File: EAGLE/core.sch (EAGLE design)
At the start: 47 parts, among them Q1 MMDT3904, U1 MIC5219, U3 STM32F10XCXT6, U4 SST25VF040B-50-4I-S2AF, X1 USB-MICROB, Y1 8Mhz

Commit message: Integrated Satish's feedback
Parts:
- removed R10: 1K, SparkFun-Passives:RESISTOR0402-RES
- R3: value 1K -> 1K5
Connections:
- removed net N$8: R4.2, X1.D+
- net BTN: now also U3PORTB_H.PB11
- net GND: now also C5.1, RESET.1; no longer R10.1, U3PORTB_H.PB11
- net N$1: now also R3.1, R4.2, X1.D+; no longer C5.1, R10.2, RESET.1
- net N$6: no longer R3.1
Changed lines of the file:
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@@
 <setting verticaltext="up"/>
 </settings>
-<grid distance="0.1" unitdist="inch" unit="inch" style="lines" multiple="1" display="no" altdistance="0.005" altunitdist="inch" altunit="inch"/>
+<grid distance="0.05" unitdist="inch" unit="inch" style="lines" multiple="1" display="yes" altdistance="0.005" altunitdist="inch" altunit="inch"/>
 <layers>
 <layer number="1" name="Top" color="4" fill="1" visible="no" active="no"/>
@@
 <part name="RESET" library="okie" deviceset="BUTTON-KMR241GLFS" device="" value="KMR211GLFS"/>
 <part name="R12" library="SparkFun-Passives" deviceset="RESISTOR" device="0402-RES" value="10K"/>
-<part name="R10" library="SparkFun-Passives" deviceset="RESISTOR" device="0402-RES" value="1K"/>
 <part name="BTN" library="okie" deviceset="BUTTON-KMR241GLFS" device="" value="KMR211GLFS"/>
 <part name="R15" library="SparkFun" deviceset="RESISTOR" device="0402-RES" value="1K"/>
@@
 <part name="R1" library="SparkFun" deviceset="RESISTOR" device="0402-RES" value="10K"/>
 <part name="+3V6" library="supply1" deviceset="+3V3" device=""/>
-<part name="R3" library="SparkFun" deviceset="RESISTOR" device="0402-RES" value="1K"/>
+<part name="R3" library="SparkFun" deviceset="RESISTOR" device="0402-RES" value="1K5"/>
 <part name="GND17" library="supply1" deviceset="GND" device=""/>
 <part name="C10" library="SparkFun-Capacitors" deviceset="CAP" device="0402-CAP" value="100nF"/>
@@
 <attribute name="VALUE" x="304.292" y="67.31" size="1.778" layer="96" rot="R90"/>
 </instance>
-<instance part="R10" gate="G$1" x="265.43" y="49.53" smashed="yes" rot="R90">
-<attribute name="NAME" x="263.9314" y="46.99" size="1.778" layer="95" rot="R90"/>
-<attribute name="VALUE" x="268.732" y="46.99" size="1.778" layer="96" rot="R90"/>
-</instance>
 <instance part="BTN" gate="G$1" x="295.91" y="21.59" smashed="yes">
 <attribute name="NAME" x="293.37" y="26.67" size="1.778" layer="95"/>
@@
 </segment>
 <segment>
-<pinref part="R10" gate="G$1" pin="1"/>
-<pinref part="GND12" gate="1" pin="GND"/>
-</segment>
-<segment>
 <pinref part="R11" gate="G$1" pin="2"/>
 <pinref part="GND13" gate="1" pin="GND"/>
@@
 <wire x1="259.08" y1="99.06" x2="264.16" y2="99.06" width="0.1524" layer="91"/>
 <junction x="264.16" y="99.06"/>
-<pinref part="U3" gate="PORTB_H" pin="PB11"/>
-<wire x1="299.72" y1="157.48" x2="259.08" y2="157.48" width="0.1524" layer="91"/>
-<wire x1="259.08" y1="157.48" x2="259.08" y2="149.86" width="0.1524" layer="91"/>
 <junction x="259.08" y="127"/>
 <pinref part="U3" gate="PORTB_H" pin="PB8"/>
 <wire x1="259.08" y1="149.86" x2="259.08" y2="127" width="0.1524" layer="91"/>
 <wire x1="299.72" y1="149.86" x2="259.08" y2="149.86" width="0.1524" layer="91"/>
-<junction x="259.08" y="149.86"/>
 </segment>
 <segment>
@@
 <wire x1="447.04" y1="167.64" x2="457.2" y2="167.64" width="0.1524" layer="91"/>
 <wire x1="457.2" y1="167.64" x2="457.2" y2="162.56" width="0.1524" layer="91"/>
+</segment>
+<segment>
+<wire x1="267.97" y1="62.23" x2="265.43" y2="62.23" width="0.1524" layer="91"/>
+<wire x1="265.43" y1="62.23" x2="265.43" y2="55.88" width="0.1524" layer="91"/>
+<pinref part="RESET" gate="G$1" pin="1"/>
+<pinref part="C5" gate="G$1" pin="1"/>
+<wire x1="279.4" y1="55.88" x2="265.43" y2="55.88" width="0.1524" layer="91"/>
+<junction x="265.43" y="55.88"/>
+<pinref part="GND12" gate="1" pin="GND"/>
+<wire x1="265.43" y1="55.88" x2="265.43" y2="44.45" width="0.1524" layer="91"/>
 </segment>
 </net>
@@
 <wire x1="15.24" y1="83.82" x2="22.86" y2="83.82" width="0.1524" layer="91"/>
 <wire x1="22.86" y1="83.82" x2="22.86" y2="81.28" width="0.1524" layer="91"/>
-<wire x1="22.86" y1="81.28" x2="74.93" y2="81.28" width="0.1524" layer="91"/>
+<wire x1="22.86" y1="81.28" x2="88.9" y2="81.28" width="0.1524" layer="91"/>
 <pinref part="R5" gate="G$1" pin="2"/>
 <pinref part="X1" gate="G$1" pin="D-"/>
-<pinref part="R3" gate="G$1" pin="1"/>
-<wire x1="74.93" y1="81.28" x2="88.9" y2="81.28" width="0.1524" layer="91"/>
-<wire x1="72.39" y1="67.31" x2="74.93" y2="67.31" width="0.1524" layer="91"/>
-<wire x1="74.93" y1="67.31" x2="74.93" y2="81.28" width="0.1524" layer="91"/>
-<junction x="74.93" y="81.28"/>
-</segment>
-</net>
-<net name="N$8" class="0">
-<segment>
-<wire x1="15.24" y1="86.36" x2="22.86" y2="86.36" width="0.1524" layer="91"/>
-<wire x1="22.86" y1="86.36" x2="22.86" y2="88.9" width="0.1524" layer="91"/>
-<wire x1="22.86" y1="88.9" x2="88.9" y2="88.9" width="0.1524" layer="91"/>
-<pinref part="R4" gate="G$1" pin="2"/>
-<pinref part="X1" gate="G$1" pin="D+"/>
 </segment>
 </net>
@@
 </segment>
 </net>
-<net name="N$1" class="0">
-<segment>
-<wire x1="267.97" y1="62.23" x2="265.43" y2="62.23" width="0.1524" layer="91"/>
-<wire x1="265.43" y1="62.23" x2="265.43" y2="55.88" width="0.1524" layer="91"/>
-<pinref part="RESET" gate="G$1" pin="1"/>
-<pinref part="R10" gate="G$1" pin="2"/>
-<pinref part="C5" gate="G$1" pin="1"/>
-<wire x1="265.43" y1="55.88" x2="265.43" y2="54.61" width="0.1524" layer="91"/>
-<wire x1="279.4" y1="55.88" x2="265.43" y2="55.88" width="0.1524" layer="91"/>
-<junction x="265.43" y="55.88"/>
-</segment>
-</net>
 <net name="N$2" class="0">
 <segment>
@@
 <wire x1="285.75" y1="12.7" x2="285.75" y2="21.59" width="0.1524" layer="91"/>
 <junction x="285.75" y="21.59"/>
+</segment>
+<segment>
+<pinref part="U3" gate="PORTB_H" pin="PB11"/>
+<wire x1="299.72" y1="157.48" x2="261.62" y2="157.48" width="0.1524" layer="91"/>
+<label x="261.62" y="157.48" size="1.778" layer="95"/>
 </segment>
 </net>
@@
 </segment>
 </net>
+<net name="N$1" class="0">
+<segment>
+<pinref part="R3" gate="G$1" pin="1"/>
+<wire x1="72.39" y1="67.31" x2="74.93" y2="67.31" width="0.1524" layer="91"/>
+<wire x1="15.24" y1="86.36" x2="22.86" y2="86.36" width="0.1524" layer="91"/>
+<wire x1="22.86" y1="86.36" x2="22.86" y2="88.9" width="0.1524" layer="91"/>
+<wire x1="22.86" y1="88.9" x2="74.93" y2="88.9" width="0.1524" layer="91"/>
+<pinref part="R4" gate="G$1" pin="2"/>
+<pinref part="X1" gate="G$1" pin="D+"/>
+<wire x1="74.93" y1="88.9" x2="88.9" y2="88.9" width="0.1524" layer="91"/>
+<wire x1="74.93" y1="67.31" x2="74.93" y2="88.9" width="0.1524" layer="91"/>
+<junction x="74.93" y="88.9"/>
+</segment>
+</net>

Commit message: Updated with Andy's feedback
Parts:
- removed R11: 10K, SparkFun-Passives:RESISTOR0402-RES
- removed R13: 1K, SparkFun-Passives:RESISTOR0402-RES
- added C13: 100nF, SparkFun-Capacitors:CAP0402-CAP
- added L2: BLM15HB121SN1, inductors:BLM15HB121SN1
- C6: value 100nF -> 10uF; device SparkFun-Capacitors:CAP0402-CAP -> SparkFun:CAP_POL1206
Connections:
- removed net N$14: BTN.2, C6.2, R13.1
- new net VDDA: C13.1, C6.+, JP2.3, L2.2, U3AN_POWER.VDDA
- net +3V3: now also L2.1; no longer R13.2, U3AN_POWER.VDDA
- net BTN: now also BTN.2, U3PORTA_H.PA10; no longer BTN.1, C6.1, R11.1, U3PORTB_H.PB11
- net GND: now also BTN.1, C13.2, C6.-; no longer JP2.3, R11.2, U3PORTA_H.PA10, U3PORTB_H.PB8, U3PORTB_L.PB2
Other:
- moved on the sheet: C10, C11, C12

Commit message: Made all board revisions. Time for production
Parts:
- added R10: 1K, rcl:R-US_R0603
- C10, C11, C12, C13, C3, C4, C5, C7, C8, C9: device SparkFun-Capacitors:CAP0402-CAP -> rcl:C-EUC0603
- L1: device SparkFun-Passives:INDUCTOR0402 -> SparkFun-Passives:INDUCTOR0603
- L2: value BLM15HB121SN1 -> Ferrite Bead; device inductors:BLM15HB121SN1 -> SparkFun-Passives:INDUCTOR0603
- R1, R14, R15, R16, R2, R3, R4, R5, R6, R7, R8, R9: device SparkFun:RESISTOR0402-RES -> rcl:R-US_R0603
- R12: device SparkFun-Passives:RESISTOR0402-RES -> rcl:R-US_R0603
- X1: device SparkFun:USB-MICROB -> SparkFun-Connectors:USB-MICROB
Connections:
- new net N$8: Q1G$2.B, R10.2
- net +3V3: now also U4.HOLD, U4.WP
- net USB_DISC: now also R10.1; no longer Q1G$2.B
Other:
- moved on the sheet: C10, C11, C12, C13, C3, C4, C5, C7, C8, C9

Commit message: Re-numbered components
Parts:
- removed R16: 1K, rcl:R-US_R0603
- added R11: 10K, rcl:R-US_R0603
- C12: value 100nF -> 10uF; device rcl:C-EUC0603 -> SparkFun:CAP_POL1206
- C6: value 10uF -> 100nF; device SparkFun:CAP_POL1206 -> rcl:C-EUC0603
- R10: value 1K -> 10K
- R12, R8: value 10K -> 1K
- R4: value 22 -> 1K
- R6: value 47K -> 22
- R7: value 1K -> 47K
- renumbered R15 to R13
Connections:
- net !RST: now also R11.1; no longer R12.1
- net +3V3: now also C6.1, R11.2, R14.2, R7.1, R9.2; no longer C12.1, R12.2, R16.2, R6.1, R7.2
- net GND: now also C12.-, C6.2, R10.1; no longer C12.2, C6.-, R9.1
- net LED1: now also R12.2; no longer R14.2
- net MEM_CS: now also R14.1; no longer R16.1
- net N$1: now also R5.2; no longer R4.2
- net N$2: now also R12.1; no longer R14.1
- net N$38: now also R8.1; no longer R7.1
- net N$6: now also R6.2; no longer R5.2
- net N$8: now also R4.2; no longer R10.2
- net USBM: now also R6.1; no longer R5.1
- net USBP: now also R5.1; no longer R4.1
- net USB_DISC: now also R4.1, R7.2; no longer R10.1, R6.2
- net VDDA: now also C12.+; no longer C6.+
- net WIFI_CS: now also R9.1; no longer R8.1
- net WIFI_EN: now also R10.2; no longer R9.2
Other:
- moved on the sheet: C10, C11, C7, R10, R12, R14, R4, R5, R6, R7, R8, R9

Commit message: Cleaned up schematic
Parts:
- L2: value Ferrite Bead -> Bead
- LED2, LED3: value Red -> Blue
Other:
- note added: "VDDA"
- note added: "Wi-Fi Module"
- moved on the sheet: A1, BTN, C12, C3, C4, C5, C6, L1, LED2, LED3, R10, R11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

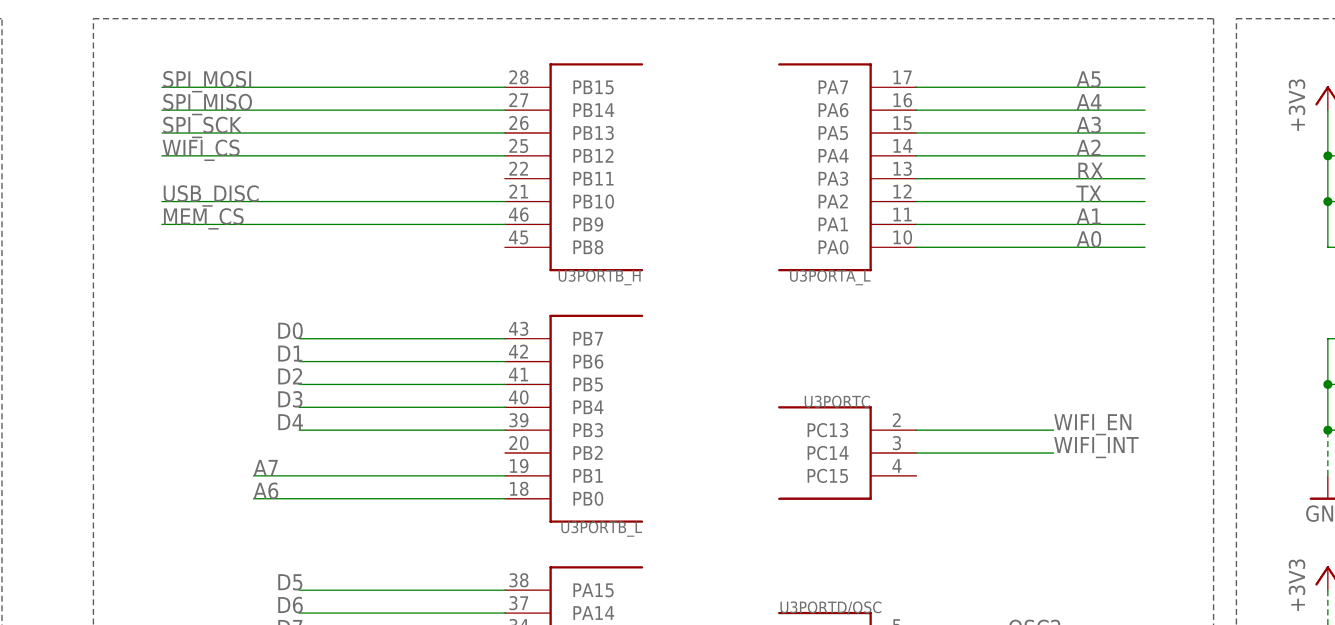
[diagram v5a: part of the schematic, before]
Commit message: Updated EAGLE files with new WIFI_EN and WIFI_INT pins and better grounding
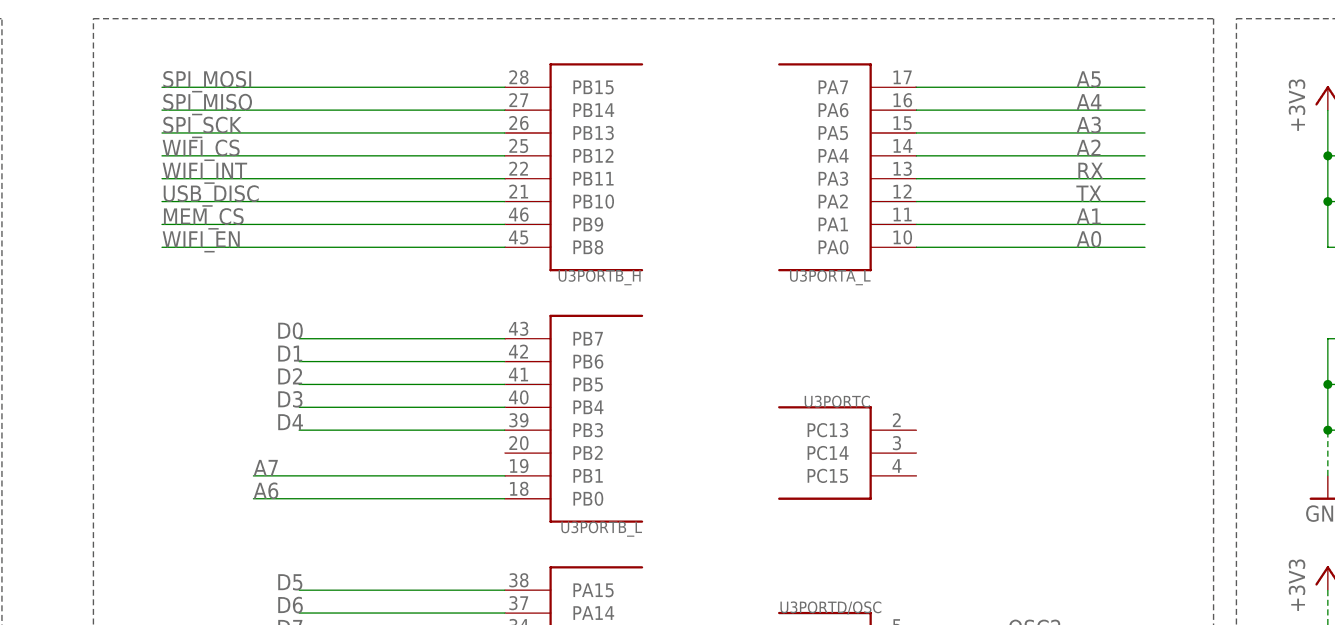
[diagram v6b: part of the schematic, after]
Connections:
- net WIFI_EN: now also U3PORTB_H.PB8; no longer U3PORTC.PC13
- net WIFI_INT: now also U3PORTB_H.PB11; no longer U3PORTC.PC14
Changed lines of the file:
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@@
 </segment>
 <segment>
-<pinref part="U3" gate="PORTC" pin="PC14"/>
-<wire x1="347.98" y1="134.62" x2="363.22" y2="134.62" width="0.1524" layer="91"/>
-<label x="363.22" y="134.62" size="1.778" layer="95"/>
+<pinref part="U3" gate="PORTB_H" pin="PB11"/>
+<wire x1="302.26" y1="165.1" x2="264.16" y2="165.1" width="0.1524" layer="91"/>
+<label x="264.16" y="165.1" size="1.778" layer="95"/>
 </segment>
 </net>
@@
 </segment>
 <segment>
-<pinref part="U3" gate="PORTC" pin="PC13"/>
-<wire x1="347.98" y1="137.16" x2="363.22" y2="137.16" width="0.1524" layer="91"/>
-<label x="363.22" y="137.16" size="1.778" layer="95"/>
+<pinref part="U3" gate="PORTB_H" pin="PB8"/>
+<wire x1="302.26" y1="157.48" x2="264.16" y2="157.48" width="0.1524" layer="91"/>
+<label x="264.16" y="157.48" size="1.778" layer="95"/>
 </segment>
 </net>

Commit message: Finished Core Debug v0.0.8
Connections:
- net SPI_MISO: no longer U2.SPI_DIN
- net SPI_MOSI: now also U2.SPI_DIN
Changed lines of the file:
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@@
 <setting verticaltext="up"/>
 </settings>
-<grid distance="0.05" unitdist="inch" unit="inch" style="lines" multiple="1" display="yes" altdistance="0.005" altunitdist="inch" altunit="inch"/>
+<grid distance="0.1" unitdist="inch" unit="inch" style="lines" multiple="1" display="no" altdistance="0.01" altunitdist="inch" altunit="inch"/>
 <layers>
 <layer number="1" name="Top" color="4" fill="1" visible="no" active="no"/>
@@
 </segment>
 <segment>
-<pinref part="U2" gate="G$1" pin="SPI_DIN"/>
-<wire x1="180.34" y1="91.44" x2="180.34" y2="76.2" width="0.1524" layer="91"/>
-<label x="180.34" y="68.58" size="1.778" layer="95" rot="R90"/>
-</segment>
-<segment>
 <pinref part="U3" gate="PORTB_H" pin="PB14"/>
 <wire x1="302.26" y1="172.72" x2="264.16" y2="172.72" width="0.1524" layer="91"/>
@@
 <label x="441.96" y="71.12" size="1.778" layer="95"/>
 </segment>
-</net>
+<segment>
+<pinref part="U2" gate="G$1" pin="SPI_DIN"/>
+<wire x1="180.34" y1="91.44" x2="180.34" y2="76.2" width="0.1524" layer="91"/>
+<label x="180.34" y="68.58" size="1.778" layer="95" rot="R90"/>
+</segment>
+</net>
